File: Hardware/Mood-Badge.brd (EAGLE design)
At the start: 100 x 80 mm, 16 parts, among them J1 AVR_SPI_PROG_3X2NS, J2 FTDI_DEVICE, SW2 SWITCH.JS202011JXQNUPWARDS, U1 ATMEGA328P_TQFP, U2 MIC550X

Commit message: day 3 changs
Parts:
- added C3, C4, C7: (no value), LinnesLab-Passives:C0603
- added D2: (no value), LinnesLab-DiscreteSemi:USC
- added R2: (no value), LinnesLab-Passives:R0603
- added U3: MCP73831.SOT23-5, LinnesLab-Power:SOT23-5
- added USB1: USB.MICRO-BIGGERPADS, LinnesLab-Connectors:USB-MICRO-01.BIGGERPADS
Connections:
- net N$2 renamed VLIPO
- removed net N$5: D1.-, U2.1
- new net VBAT: U3.3
- new net VIN: C3.1, C7.1, D1.-, D2.-, R2.2, U2.1, U2.3, U3.4
- new net VSS: U3.2
- new net V_USB: D2.+, USB1.1
- net 3.3V: now also C4.1, U2.5
- net GND: now also C3.2, C4.2, C7.2, U2.2, USB1.5, USB1.S1, USB1.S2, USB1.S3, USB1.S4, USB1.S5, USB1.S6
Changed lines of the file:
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@@
 <attribute name="VALUE" x="-59.69" y="-62.23" size="0.6096" layer="27" ratio="20" rot="R90" align="bottom-center"/>
+</element>
+<element name="C3" library="LinnesLab-Passives" package="C0603" package3d_urn="urn:adsk.eagle:package:15661989/2" value="" x="-63.5" y="-66.04" smashed="yes">
+<attribute name="NAME" x="-64.135" y="-65.405" size="0.7112" layer="25"/>
+<attribute name="VALUE" x="-64.135" y="-67.945" size="0.7112" layer="27"/>
+</element>
+<element name="C4" library="LinnesLab-Passives" package="C0603" package3d_urn="urn:adsk.eagle:package:15661989/2" value="" x="-63.5" y="-69.85" smashed="yes">
+<attribute name="NAME" x="-64.135" y="-69.215" size="0.7112" layer="25"/>
+<attribute name="VALUE" x="-64.135" y="-71.755" size="0.7112" layer="27"/>
+</element>
+<element name="USB1" library="LinnesLab-Connectors" package="USB-MICRO-01.BIGGERPADS" package3d_urn="urn:adsk.eagle:package:36706858/2" value="USB.MICRO-BIGGERPADS" x="-58.42" y="-74.93" smashed="yes">
+<attribute name="NAME" x="-62.23" y="-72.136" size="0.7112" layer="25"/>
+<attribute name="VALUE" x="-57.15" y="-72.136" size="0.7112" layer="27"/>
+</element>
+<element name="D2" library="LinnesLab-DiscreteSemi" package="USC" package3d_urn="urn:adsk.eagle:package:15664784/2" value="" x="-67.31" y="-76.2" smashed="yes">
+<attribute name="NAME" x="-68.58" y="-75.1" size="0.635" layer="25"/>
+<attribute name="VALUE" x="-68.58" y="-77.865" size="0.635" layer="27"/>
+</element>
+<element name="C7" library="LinnesLab-Passives" package="C0603" package3d_urn="urn:adsk.eagle:package:15661989/2" value="" x="-67.31" y="-81.28" smashed="yes">
+<attribute name="NAME" x="-67.945" y="-80.645" size="0.7112" layer="25"/>
+<attribute name="VALUE" x="-67.945" y="-83.185" size="0.7112" layer="27"/>
+</element>
+<element name="R2" library="LinnesLab-Passives" package="R0603" package3d_urn="urn:adsk.eagle:package:15661944/2" value="" x="-67.31" y="-85.09" smashed="yes">
+<attribute name="NAME" x="-67.945" y="-84.455" size="0.7112" layer="25"/>
+<attribute name="VALUE" x="-67.945" y="-86.995" size="0.7112" layer="27"/>
+</element>
+<element name="U3" library="LinnesLab-Power" package="SOT23-5" package3d_urn="urn:adsk.eagle:package:18172171/2" value="MCP73831.SOT23-5" x="-66.04" y="-88.9" smashed="yes">
+<attribute name="NAME" x="-67.945" y="-88.9" size="0.6096" layer="25" ratio="20" rot="R90" align="bottom-center"/>
+<attribute name="VALUE" x="-63.5" y="-88.9" size="0.6096" layer="27" ratio="20" rot="R90" align="bottom-center"/>
 </element>
 </elements>
@@
 <contactref element="J2" pad="CTS"/>
 <contactref element="LIPO1" pad="1"/>
+<contactref element="C3" pad="2"/>
+<contactref element="U2" pad="2"/>
+<contactref element="C4" pad="2"/>
+<contactref element="USB1" pad="S6"/>
+<contactref element="USB1" pad="S2"/>
+<contactref element="USB1" pad="S1"/>
+<contactref element="USB1" pad="S5"/>
+<contactref element="USB1" pad="S3"/>
+<contactref element="USB1" pad="S4"/>
+<contactref element="USB1" pad="5"/>
+<contactref element="C7" pad="2"/>
+<wire x1="-62.27" y1="-76.2" x2="-66.46" y2="-81.28" width="0" layer="19" extent="1-1"/>
+<wire x1="-59.62" y1="-76.2" x2="-62.27" y2="-76.2" width="0" layer="19" extent="1-1"/>
+<wire x1="-57.22" y1="-76.2" x2="-59.62" y2="-76.2" width="0" layer="19" extent="1-1"/>
+<wire x1="-61.52" y1="-73.65" x2="-62.27" y2="-76.2" width="0" layer="19" extent="1-1"/>
+<wire x1="-54.57" y1="-76.2" x2="-57.22" y2="-76.2" width="0" layer="19" extent="1-1"/>
+<wire x1="-55.32" y1="-73.65" x2="-54.57" y2="-76.2" width="0" layer="19" extent="1-1"/>
+<wire x1="-57.12" y1="-73.425" x2="-55.32" y2="-73.65" width="0" layer="19" extent="1-1"/>
+<wire x1="-62.65" y1="-69.85" x2="-61.52" y2="-73.65" width="0" layer="19" extent="1-1"/>
+<wire x1="-62.65" y1="-66.04" x2="-62.65" y2="-69.85" width="0" layer="19" extent="1-1"/>
+<wire x1="-62.23" y1="-63.5301" x2="-62.65" y2="-66.04" width="0" layer="19" extent="1-1"/>
+<wire x1="-56.88" y1="-45.61" x2="-62.23" y2="-63.5301" width="0" layer="19" extent="1-1"/>
 <wire x1="-38.1" y1="-46.99" x2="-56.88" y2="-45.61" width="0" layer="19" extent="1-1"/>
 <wire x1="-35.56" y1="-46.99" x2="-38.1" y2="-46.99" width="0" layer="19" extent="1-1"/>
@@
 <contactref element="J1" pad="2"/>
 <contactref element="J2" pad="VCC"/>
+<contactref element="C4" pad="1"/>
+<contactref element="U2" pad="5"/>
+<wire x1="-63.18" y1="-60.9299" x2="-64.35" y2="-69.85" width="0" layer="19" extent="1-1"/>
+<wire x1="-40.64" y1="-46.99" x2="-63.18" y2="-60.9299" width="0" layer="19" extent="1-1"/>
 <wire x1="-11.43" y1="-38.1" x2="-40.64" y2="-46.99" width="0" layer="19" extent="1-1"/>
 <wire x1="-13.55" y1="-25.4" x2="-11.43" y2="-38.1" width="0" layer="19" extent="1-1"/>
@@
 <wire x1="-0.7874" y1="4.82" x2="-22.86" y2="-12.13" width="0" layer="19" extent="1-1"/>
 </signal>
-<signal name="N$2">
-<contactref element="LIPO1" pad="2"/>
-<contactref element="SW2" pad="2"/>
-<wire x1="-54.88" y1="-45.61" x2="-54.61" y2="-50.47" width="0" layer="19" extent="1-1"/>
-</signal>
 <signal name="N$3">
 <contactref element="SW2" pad="1"/>
@@
 <wire x1="-57.11" y1="-50.47" x2="-64.65" y2="-57.15" width="0" layer="19" extent="1-1"/>
 </signal>
-<signal name="N$5">
+<signal name="VLIPO">
+<contactref element="LIPO1" pad="2"/>
+<contactref element="SW2" pad="2"/>
+<wire x1="-54.88" y1="-45.61" x2="-54.61" y2="-50.47" width="0" layer="19" extent="1-1"/>
+</signal>
+<signal name="VIN">
 <contactref element="D1" pad="-"/>
 <contactref element="U2" pad="1"/>
+<contactref element="U2" pad="3"/>
+<contactref element="C3" pad="1"/>
+<contactref element="D2" pad="-"/>
+<contactref element="C7" pad="1"/>
+<contactref element="U3" pad="4"/>
+<contactref element="R2" pad="2"/>
+<wire x1="-66.46" y1="-85.09" x2="-65.09" y2="-87.5999" width="0" layer="19" extent="1-1"/>
+<wire x1="-68.16" y1="-81.28" x2="-66.46" y2="-85.09" width="0" layer="19" extent="1-1"/>
+<wire x1="-66.16" y1="-76.2" x2="-68.16" y2="-81.28" width="0" layer="19" extent="1-1"/>
+<wire x1="-64.35" y1="-66.04" x2="-66.16" y2="-76.2" width="0" layer="19" extent="1-1"/>
+<wire x1="-63.18" y1="-63.5301" x2="-64.35" y2="-66.04" width="0" layer="19" extent="1-1"/>
+<wire x1="-61.28" y1="-63.5301" x2="-63.18" y2="-63.5301" width="0" layer="19" extent="1-1"/>
 <wire x1="-62.35" y1="-57.15" x2="-63.18" y2="-63.5301" width="0" layer="19" extent="1-1"/>
 </signal>
+<signal name="V_USB">
+<contactref element="USB1" pad="1"/>
+<contactref element="D2" pad="+"/>
+<wire x1="-59.72" y1="-73.425" x2="-68.46" y2="-76.2" width="0" layer="19" extent="1-1"/>
+</signal>
+<signal name="VBAT">
+<contactref element="U3" pad="3"/>
+</signal>
+<signal name="VSS">
+<contactref element="U3" pad="2"/>
+</signal>
 </signals>

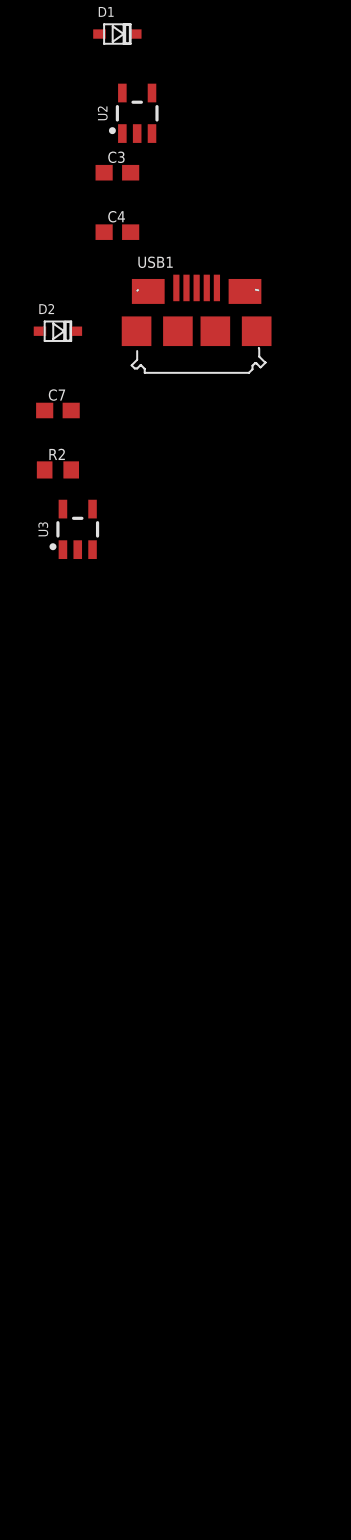
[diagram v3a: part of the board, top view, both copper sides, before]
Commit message: the schematic is ready, the LED for the power managemnet circuit should still be added.
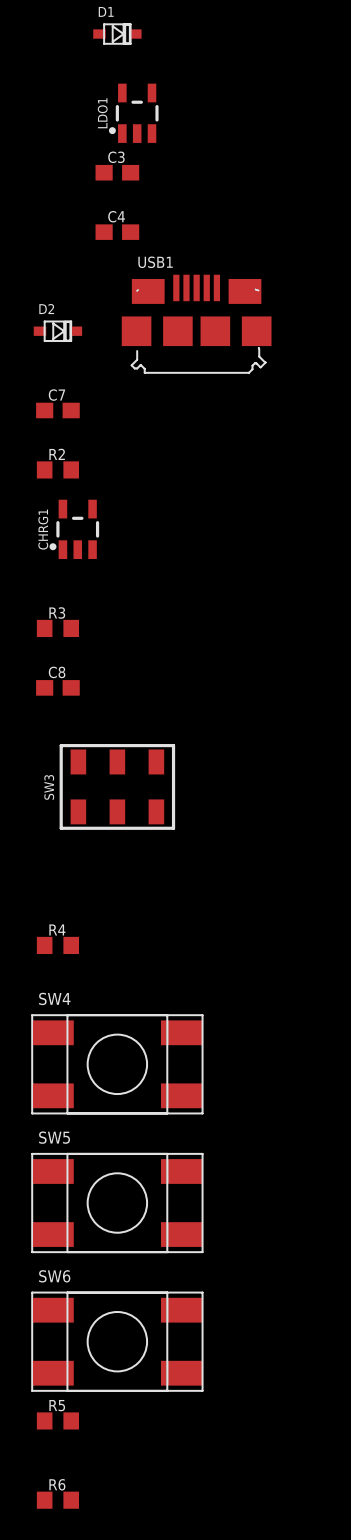
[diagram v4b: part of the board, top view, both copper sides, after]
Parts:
- added C8: 4.7u, LinnesLab-Passives:C0603
- added R3: (no value), LinnesLab-Passives:R0603
- added R4, R5, R6: 10k, LinnesLab-Passives:R0603
- added SW3: SWITCH.JS202011JXQNUPWARDS, LinnesLab-Switches:SWITCH.00
- added SW4, SW5, SW6: (no value), LinnesLab-Switches:SPST.KT11P4SM34LFS
- C3, C4: value (none) -> 1u
- C7: value (none) -> 4.7u
- R2: value (none) -> 100k
- renumbered U2 to LDO1, U3 to CHRG1
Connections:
- removed net VBAT: CHRG1.3
- removed net VSS: CHRG1.2
- new net CHRG.STAT: R2.1
- new net N$5: CHRG1.5, R3.2
- net 3.3V: now also SW3.1, SW4.1, SW4.2, SW5.1, SW5.2, SW6.1, SW6.2
- net ACTION: now also R6.2, SW4.3, SW4.4
- net GND: now also C8.2, CHRG1.2, R3.1, R4.1, R5.1, R6.1, SW3.3
- net LEFT: now also R4.2, SW5.3, SW5.4
- net MODE: now also SW3.2
- net RIGHT: now also R5.2, SW6.3, SW6.4
- net VLIPO: now also C8.1, CHRG1.3

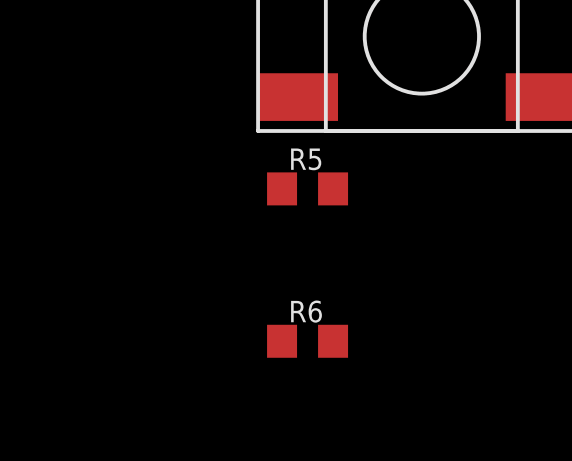
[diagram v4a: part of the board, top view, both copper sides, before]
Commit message: added LED
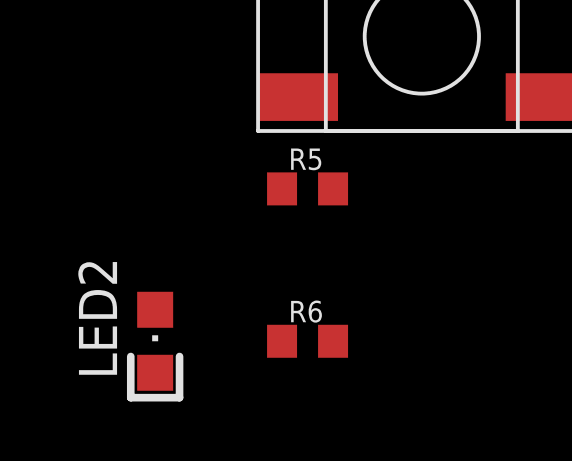
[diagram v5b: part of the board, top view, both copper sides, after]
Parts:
- added LED2: (no value), LinnesLab-LED:LED-0805
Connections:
- new net N$2: CHRG1.1, LED2.C
- net CHRG.STAT: now also LED2.A
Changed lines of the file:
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@@
 <layer number="146" name="DrillLegend_01-20" color="7" fill="1" visible="yes" active="yes"/>
 <layer number="147" name="PIN_NUMBER" color="7" fill="1" visible="yes" active="yes"/>
+<layer number="148" name="mDocument" color="7" fill="1" visible="yes" active="yes"/>
 <layer number="149" name="DrillLegend_02-15" color="7" fill="1" visible="yes" active="yes"/>
 <layer number="150" name="Notes" color="7" fill="1" visible="yes" active="yes"/>
@@
 <attribute name="VALUE" x="-67.945" y="-153.035" size="0.7112" layer="27"/>
 </element>
+<element name="LED2" library="LinnesLab-LED" package="LED-0805" value="" x="-72.39" y="-151.13" smashed="yes">
+<attribute name="NAME" x="-73.66" y="-152.4" size="1.27" layer="25" rot="R90"/>
+<attribute name="VALUE" x="-69.85" y="-152.4" size="1.27" layer="27" rot="R90"/>
+</element>
 </elements>
 <signals>
@@
 <signal name="CHRG.STAT">
 <contactref element="R2" pad="1"/>
+<contactref element="LED2" pad="A"/>
+<wire x1="-68.16" y1="-85.09" x2="-72.39" y2="-152.18" width="0" layer="19" extent="1-1"/>
 </signal>
 <signal name="N$5">
@@
 <wire x1="-66.99" y1="-87.5999" x2="-66.46" y2="-95.25" width="0" layer="19" extent="1-1"/>
 </signal>
+<signal name="N$2">
+<contactref element="LED2" pad="C"/>
+<contactref element="CHRG1" pad="1"/>
+<wire x1="-66.99" y1="-90.2001" x2="-72.39" y2="-150.08" width="0" layer="19" extent="1-1"/>
+</signal>
 </signals>

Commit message: board layout done, wiring is in progress
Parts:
- moved R5 227.6 mm to (21.6, 63.5), turned to 90 degrees
- moved LED2 224.6 mm to (71.1, 21.6), turned to 180 degrees
- moved SW6 217.3 mm to (10.2, 63.5)
- moved R6 214.2 mm to (22.9, 43.2), turned to 270 degrees
- moved SW5 203.5 mm to (20.3, 53.3)
- moved R4 184.1 mm to (8.89, 52.1), turned to 90 degrees
- moved SW4 181.9 mm to (10.2, 43.2)
- moved R2 177.8 mm to (74.9, 21.6), turned to 90 degrees
- moved SW3 176.1 mm to (57.1, 22.9)
- moved C8 176.0 mm to (73.7, 6.35), turned to 180 degrees
- moved CHRG1 173.5 mm to (73.7, 14.0), turned to 90 degrees
- moved R3 169.7 mm to (68.6, 6.35)
- moved C7 162.6 mm to (63.5, 15.2)
- moved D2 152.2 mm to (57.1, 11.4), turned to 90 degrees
- moved USB1 140.2 mm to (58.4, 2.54)
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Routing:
- net LD10: track 0.00 -> 92.4 mm
- net LD9: track 0.00 -> 83.4 mm
- net LD11: track 0.00 -> 69.7 mm, vias 0 -> 3
- net LD12: track 0.00 -> 62.8 mm, vias 0 -> 2
- net RXD: track 0.00 -> 51.5 mm
- net TXD: track 0.00 -> 43.8 mm
- net RESET: track 0.00 -> 30.9 mm
- net VIN: track 0.00 -> 29.3 mm
- net DTR: track 0.00 -> 24.3 mm
- net LD1: track 0.00 -> 18.3 mm, vias 0 -> 2
- net VLIPO: track 0.00 -> 18.1 mm
- net LD8: track 0.00 -> 17.6 mm, vias 0 -> 2
- net LD2: track 0.00 -> 16.1 mm, vias 0 -> 2
- net MODE: track 0.00 -> 15.7 mm
- net LD7: track 0.00 -> 13.6 mm
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
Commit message: wiring is done
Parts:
- moved SW4 71.2 mm to (80.0, 29.2)
- moved R5 71.0 mm to (91.4, 50.8), turned to 180 degrees
- moved R6 70.0 mm to (91.4, 29.2), turned to 180 degrees
- moved SW5 69.7 mm to (88.9, 40.6)
- moved SW6 69.7 mm to (78.7, 50.8)
- moved R4 69.5 mm to (77.5, 40.6), turned to 0 degrees
- moved J1 36.4 mm to (61.0, 67.3)
- moved U1 35.6 mm to (47.0, 67.3)
- moved SW1 33.0 mm to (17.8, 40.6)
- moved J2 29.2 mm to (2.54, 57.1)
- moved LED1 19.0 mm to (47.0, 40.6)
- moved Y1 16.5 mm to (12.7, 24.1)
- moved C1 14.9 mm to (17.8, 24.1)
- moved C2 14.9 mm to (17.8, 26.7)
- moved C6 14.9 mm to (22.9, 24.1)
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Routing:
- net N$1: track 3.49 -> 74.6 mm, vias 0 -> 2
- net N$4: track 3.07 -> 71.0 mm, vias 0 -> 2
- net LEFT: track 7.97 -> 68.2 mm, vias 0 -> 2
- net ACTION: track 9.06 -> 67.9 mm, vias 0 -> 2
- net LD9: track 83.4 -> 27.2 mm
- net LD10: track 92.4 -> 37.6 mm
- net MODE: track 15.7 -> 69.2 mm
- net LD12: track 62.8 -> 10.4 mm, vias 2 -> 0
- net RIGHT: track 8.49 -> 48.1 mm, vias 0 -> 2
- net LD4: track 11.8 -> 44.9 mm, vias 0 -> 2
- net LD3: track 11.8 -> 44.6 mm, vias 0 -> 2
- net LD5: track 12.2 -> 44.0 mm, vias 0 -> 2
- net LD6: track 12.9 -> 44.3 mm, vias 0 -> 2
- net LD7: track 13.6 -> 44.6 mm, vias 0 -> 2
- net LD8: track 17.6 -> 47.0 mm
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
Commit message: polygone is done
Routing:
- net RXD: track 60.1 -> 46.1 mm
- added copper zone on layer 1, net 3.3V
- added copper zone on layer 1, net GND
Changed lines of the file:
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@@
 <contactref element="R6" pad="1"/>
 <contactref element="SW3" pad="3"/>
-<wire x1="76.62" y1="40.64" x2="92.29" y2="50.8" width="0" layer="19" extent="1-1"/>
-<wire x1="92.29" y1="29.21" x2="76.62" y2="40.64" width="0" layer="19" extent="1-1"/>
-<wire x1="74.9601" y1="13.97" x2="92.29" y2="29.21" width="0" layer="19" extent="1-1"/>
-<wire x1="76.62" y1="7.62" x2="74.9601" y2="13.97" width="0" layer="19" extent="1-1"/>
-<wire x1="70.27" y1="7.62" x2="76.62" y2="7.62" width="0" layer="19" extent="1-1"/>
-<wire x1="66.89" y1="15.24" x2="74.9601" y2="13.97" width="0" layer="19" extent="1-1"/>
-<wire x1="58.38" y1="18.11" x2="66.89" y2="15.24" width="0" layer="19" extent="1-1"/>
-<wire x1="60.25" y1="3.82" x2="70.27" y2="7.62" width="0" layer="19" extent="1-1"/>
-<wire x1="58.45" y1="4.045" x2="60.25" y2="3.82" width="0" layer="19" extent="1-1"/>
-<wire x1="61" y1="1.27" x2="60.25" y2="3.82" width="0" layer="19" extent="1-1"/>
-<wire x1="58.35" y1="1.27" x2="61" y2="1.27" width="0" layer="19" extent="1-1"/>
-<wire x1="55.95" y1="1.27" x2="58.35" y2="1.27" width="0" layer="19" extent="1-1"/>
-<wire x1="53.3" y1="1.27" x2="55.95" y2="1.27" width="0" layer="19" extent="1-1"/>
-<wire x1="54.05" y1="3.82" x2="53.3" y2="1.27" width="0" layer="19" extent="1-1"/>
-<wire x1="39.1" y1="7.51" x2="54.05" y2="3.82" width="0" layer="19" extent="1-1"/>
-<wire x1="24.98" y1="7.62" x2="39.1" y2="7.51" width="0" layer="19" extent="1-1"/>
-<wire x1="19.9" y1="7.62" x2="24.98" y2="7.62" width="0" layer="19" extent="1-1"/>
-<wire x1="22.8299" y1="13.97" x2="24.98" y2="7.62" width="0" layer="19" extent="1-1"/>
-<wire x1="23.71" y1="24.13" x2="22.8299" y2="13.97" width="0" layer="19" extent="1-1"/>
-<wire x1="18.63" y1="24.13" x2="23.71" y2="24.13" width="0" layer="19" extent="1-1"/>
-<wire x1="18.63" y1="26.67" x2="18.63" y2="24.13" width="0" layer="19" extent="1-1"/>
-<wire x1="23.71" y1="33.02" x2="18.63" y2="26.67" width="0" layer="19" extent="1-1"/>
-<wire x1="21.9075" y1="38.62" x2="23.71" y2="33.02" width="0" layer="19" extent="1-1"/>
-<wire x1="13.6525" y1="38.62" x2="21.9075" y2="38.62" width="0" layer="19" extent="1-1"/>
-<wire x1="2.54" y1="50.8" x2="13.6525" y2="38.62" width="0" layer="19" extent="1-1"/>
-<wire x1="2.54" y1="53.34" x2="2.54" y2="50.8" width="0" layer="19" extent="1-1"/>
-<wire x1="59.730053125" y1="69.869634375" x2="76.62" y2="40.64" width="0" layer="19" extent="1-1"/>
-<wire x1="51.2826" y1="67.71" x2="59.730053125" y2="69.869634375" width="0" layer="19" extent="1-1"/>
-<wire x1="42.6974" y1="66.91" x2="51.2826" y2="67.71" width="0" layer="19" extent="1-1"/>
-<wire x1="42.6974" y1="68.51" x2="42.6974" y2="66.91" width="0" layer="19" extent="1-1"/>
+<polygon width="0.1524" layer="1">
+<vertex x="0" y="0"/>
+<vertex x="0" y="80.01"/>
+<vertex x="1.27" y="80.01"/>
+<vertex x="99.06" y="80.01"/>
+<vertex x="99.06" y="1.27"/>
+<vertex x="99.06" y="0"/>
+</polygon>
 </signal>
 <signal name="N$1">
@@
 <contactref element="SW4" pad="1"/>
 <contactref element="SW3" pad="1"/>
-<wire x1="84.7725" y1="42.66" x2="93.0275" y2="42.66" width="0" layer="19" extent="1-1"/>
-<wire x1="82.8675" y1="52.82" x2="84.7725" y2="42.66" width="0" layer="19" extent="1-1"/>
-<wire x1="74.6125" y1="52.82" x2="82.8675" y2="52.82" width="0" layer="19" extent="1-1"/>
-<wire x1="84.1375" y1="31.23" x2="84.7725" y2="42.66" width="0" layer="19" extent="1-1"/>
-<wire x1="75.8825" y1="31.23" x2="84.1375" y2="31.23" width="0" layer="19" extent="1-1"/>
-<wire x1="59.650259375" y1="64.790259375" x2="74.6125" y2="52.82" width="0" layer="19" extent="1-1"/>
-<wire x1="51.2826" y1="65.31" x2="59.650259375" y2="64.790259375" width="0" layer="19" extent="1-1"/>
-<wire x1="42.6974" y1="66.11" x2="51.2826" y2="65.31" width="0" layer="19" extent="1-1"/>
-<wire x1="42.6974" y1="67.71" x2="42.6974" y2="66.11" width="0" layer="19" extent="1-1"/>
-<wire x1="53.38" y1="18.11" x2="75.8825" y2="31.23" width="0" layer="19" extent="1-1"/>
-<wire x1="25.4301" y1="14.92" x2="53.38" y2="18.11" width="0" layer="19" extent="1-1"/>
-<wire x1="23.28" y1="7.62" x2="25.4301" y2="14.92" width="0" layer="19" extent="1-1"/>
-<wire x1="22.01" y1="24.13" x2="25.4301" y2="14.92" width="0" layer="19" extent="1-1"/>
-<wire x1="22.01" y1="33.02" x2="22.01" y2="24.13" width="0" layer="19" extent="1-1"/>
-<wire x1="18.63" y1="33.02" x2="22.01" y2="33.02" width="0" layer="19" extent="1-1"/>
-<wire x1="2.54" y1="55.88" x2="18.63" y2="33.02" width="0" layer="19" extent="1-1"/>
+<polygon width="0.1524" layer="1">
+<vertex x="1.27" y="78.74"/>
+<vertex x="96.52" y="78.74"/>
+<vertex x="99.06" y="76.2"/>
+<vertex x="99.06" y="1.27"/>
+<vertex x="97.79" y="0"/>
+<vertex x="0" y="0"/>
+<vertex x="0" y="77.47"/>
+</polygon>
 </signal>
 <signal name="DTR">
@@
 <wire x1="2.54" y1="58.42" x2="8.89" y2="58.42" width="0.1524" layer="1"/>
 <via x="8.89" y="58.42" extent="1-16" drill="0.35"/>
-<wire x1="8.89" y1="58.42" x2="22.86" y2="58.42" width="0.1524" layer="16"/>
 <wire x1="25.4" y1="72.39" x2="26.67" y2="73.66" width="0.1524" layer="16"/>
 <wire x1="26.67" y1="73.66" x2="46.99" y2="73.66" width="0.1524" layer="16"/>
@@
 <wire x1="45.72" y1="72.39" x2="45.72" y2="71.6726" width="0.1524" layer="1"/>
 <wire x1="45.72" y1="71.6726" x2="45.79" y2="71.6026" width="0.1524" layer="1"/>
+<wire x1="8.89" y1="58.42" x2="22.86" y2="58.42" width="0" layer="19" extent="16-16"/>
 </signal>
 <signal name="TXD">
